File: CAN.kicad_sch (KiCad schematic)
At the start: 18 parts, among them J21 CAN_IN, J22 CAN_OUT, J26 CAN_TP, U17 ADM3055E, U18 CDSOT23-T24CAN

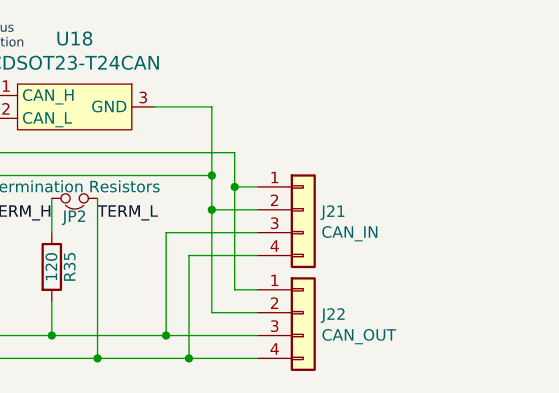
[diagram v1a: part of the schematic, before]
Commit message: Schematic notations for rework changes
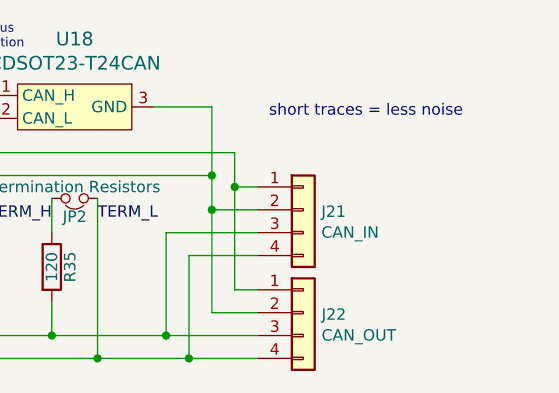
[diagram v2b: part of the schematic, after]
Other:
- note added: "short traces = less noise"

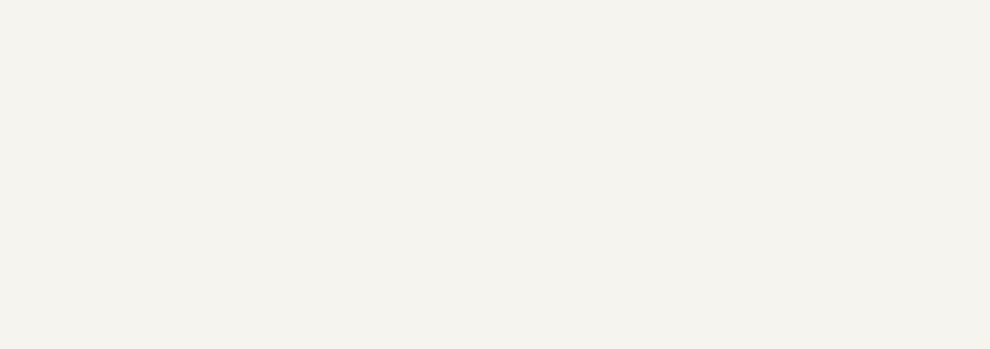
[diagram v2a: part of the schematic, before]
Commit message: Updated schematic in accordance to previous weeks annotated changes
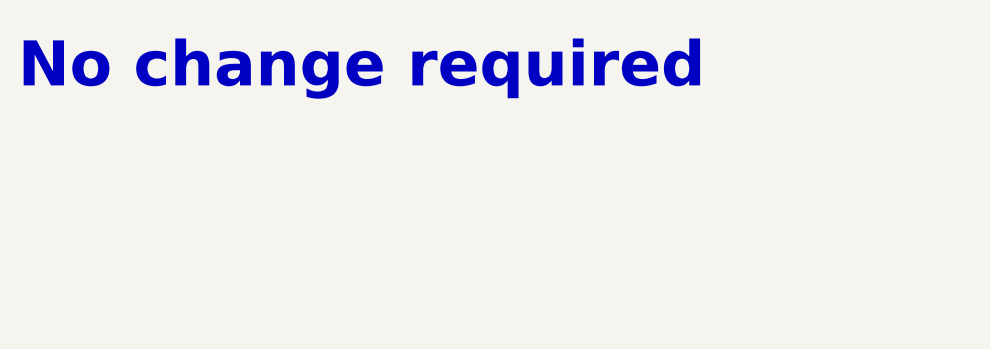
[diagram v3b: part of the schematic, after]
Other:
- note added: "No change required"
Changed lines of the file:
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@@
     (effects (font (size 1.016 1.016)) (justify left bottom))
+  )
+  (text "No change required\n" (at 15.24 21.59 0)
+    (effects (font (face "KiCad Font") (size 5 5) (thickness 1) bold (color 255 2 13 1)) (justify left bottom))
   )
   (label "TERM_L" (at 208.28 85.09 0) (fields_autoplaced)

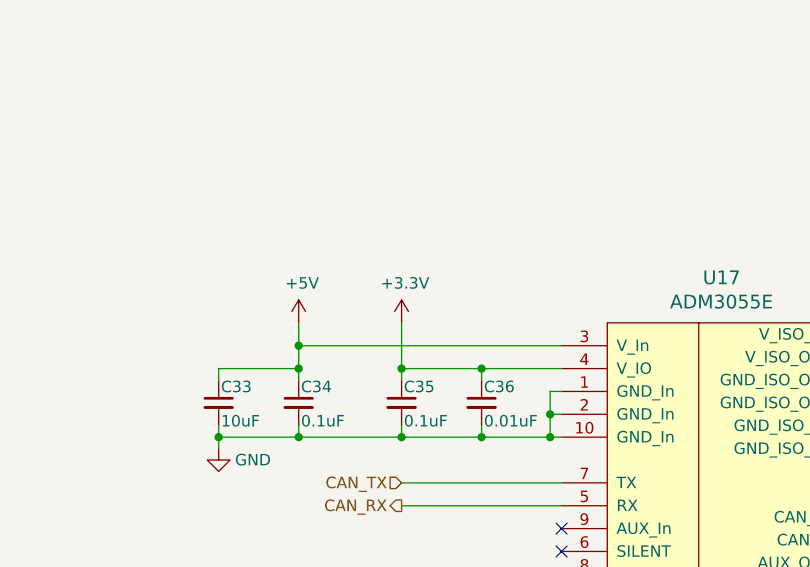
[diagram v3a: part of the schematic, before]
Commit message: Renamed Clk to PA5, removed CAN_TX/RX test points, deleted other .lck file and #auto_saved_files# (hopefully this does not break anything.
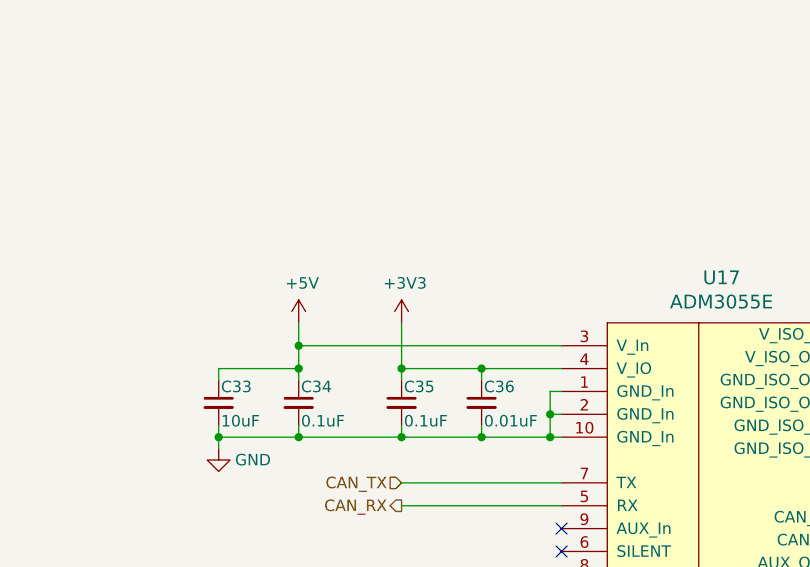
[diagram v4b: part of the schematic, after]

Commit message: Added/checked datasheet links/part numbers, deleted accel_pot2 and brake_pot2 hierarchical labels and changed corresponding pins (PC2, PC3) to GPIO on the now-2x5 extra GPIO connector.
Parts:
- C33, C38: Mouser Part Number 80-C0805C106K8RAUTO -> 963-TMK212BBJ106MGHT
- C34, C35, C39: Mouser Part Number 80-C0805C104K3R -> 80-C0805C104M5R
- C36, C40: Mouser Part Number 80-C0805X103K1R3316 -> C0805C103J5RACTU
- C37: Mouser Part Number 80-C0805C224J1RECTU -> 80-C0805C224J1RECTU
- R35: Mouser Part Number 71-CRCW080559R0FKEA -> CRCW0805120RFKEA
- U17: P/N (none) -> ADM3055E
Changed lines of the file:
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@@
 			)
 		)
-		(property "Datasheet" "~"
+		(property "Datasheet" "https://www.mouser.com/ProductDetail/71-CRCW0805120RFKEA"
 			(at 203.2 90.17 0)
 			(effects
@@
 			)
 		)
-		(property "Mouser Part Number" "71-CRCW080559R0FKEA"
+		(property "Mouser Part Number" "CRCW0805120RFKEA"
 			(at 203.2 90.17 0)
 			(effects
@@
 			)
 		)
-		(property "Datasheet" "~"
+		(property "Datasheet" "https://www.mouser.com/ProductDetail/TAIYO-YUDEN/TMK212BBJ106MGHT?qs=sGAEpiMZZMsh%252B1woXyUXj6Ion9DcW8uk%2FCsbgn7gICc%3D"
 			(at 54.61 85.09 0)
 			(effects
@@
 			)
 		)
-		(property "Mouser Part Number" "80-C0805C106K8RAUTO "
+		(property "Mouser Part Number" "963-TMK212BBJ106MGHT"
 			(at 54.61 85.09 0)
 			(effects
@@
 			)
 		)
-		(property "Datasheet" "~"
+		(property "Datasheet" "https://www.mouser.com/ProductDetail/KEMET/C0805C104M5RACTU?qs=VOOUd%252Bza08qHu13WgNByHQ%3D%3D"
 			(at 63.5 85.09 0)
 			(effects
@@
 			)
 		)
-		(property "Mouser Part Number" "80-C0805C104K3R "
+		(property "Mouser Part Number" "80-C0805C104M5R"
 			(at 63.5 85.09 0)
 			(effects
@@
 			)
 		)
-		(property "Datasheet" "~"
+		(property "Datasheet" "https://www.mouser.com/ProductDetail/KEMET/C0805C104M5RACTU?qs=VOOUd%252Bza08qHu13WgNByHQ%3D%3D"
 			(at 74.93 85.09 0)
 			(effects
@@
 			)
 		)
-		(property "Mouser Part Number" "80-C0805C104K3R "
+		(property "Mouser Part Number" "80-C0805C104M5R"
 			(at 74.93 85.09 0)
 			(effects
@@
 			)
 		)
-		(property "Datasheet" "~"
+		(property "Datasheet" "https://www.mouser.com/ProductDetail/KEMET/C0805C103J5RACTU?qs=Onq5MIl0ZjiJ615hCkQQ7A%3D%3D"
 			(at 83.82 85.09 0)
 			(effects
@@
 			)
 		)
-		(property "Mouser Part Number" "80-C0805X103K1R3316 "
+		(property "Mouser Part Number" "C0805C103J5RACTU"
 			(at 83.82 85.09 0)
 			(effects
@@
 			)
 		)
-		(property "Datasheet" "~"
+		(property "Datasheet" "https://www.mouser.com/ProductDetail/TAIYO-YUDEN/TMK212BBJ106MGHT?qs=sGAEpiMZZMsh%252B1woXyUXj6Ion9DcW8uk%2FCsbgn7gICc%3D"
 			(at 156.21 81.28 0)
 			(effects
@@
 			)
 		)
-		(property "Mouser Part Number" "80-C0805C106K8RAUTO "
+		(property "Mouser Part Number" "963-TMK212BBJ106MGHT"
 			(at 156.21 81.28 0)
 			(effects
@@
 			)
 		)
-		(property "Datasheet" "~"
+		(property "Datasheet" "https://www.mouser.com/ProductDetail/KEMET/C0805C224J1RECTU?qs=55YtniHzbhA8coEmCgZh4A%3D%3D&srsltid=AfmBOope8E98p1TAxytK4MEkGo55JjU107N1pzX-xa8_vzbWYaq6BWq_"
 			(at 146.05 81.28 0)
 			(effects
@@
 			)
 		)
-		(property "Mouser Part Number" "80-C0805C224J1RECTU "
+		(property "Mouser Part Number" "80-C0805C224J1RECTU"
 			(at 146.05 81.28 0)
 			(effects
@@
 			)
 		)
-		(property "Datasheet" ""
+		(property "Datasheet" "https://www.mouser.com/ProductDetail/TAIYO-YUDEN/BK2125LM182-T?qs=I6KAKw0tg2wTd%252Bj343lu1Q%3D%3D&srsltid=AfmBOorkhsm8Uk29brVkfBS5oJy8t8TPSw1gIhtEERu0OY8r33ydtYfJ"
 			(at 151.13 77.47 0)
 			(effects
@@
 			)
 		)
-		(property "Datasheet" ""
+		(property "Datasheet" "https://www.mouser.com/ProductDetail/TAIYO-YUDEN/BK2125LM182-T?qs=I6KAKw0tg2wTd%252Bj343lu1Q%3D%3D&srsltid=AfmBOorkhsm8Uk29brVkfBS5oJy8t8TPSw1gIhtEERu0OY8r33ydtYfJ"
 			(at 151.13 85.09 0)
 			(effects
@@
 			)
 		)
-		(property "Datasheet" "~"
+		(property "Datasheet" "https://www.mouser.com/ProductDetail/KEMET/C0805C104M5RACTU?qs=VOOUd%252Bza08qHu13WgNByHQ%3D%3D"
 			(at 166.37 81.28 0)
 			(effects
@@
 			)
 		)
-		(property "Mouser Part Number" "80-C0805C104K3R "
+		(property "Mouser Part Number" "80-C0805C104M5R"
 			(at 166.37 81.28 0)
 			(effects
@@
 			)
 		)
-		(property "Datasheet" "~"
+		(property "Datasheet" "https://www.mouser.com/ProductDetail/KEMET/C0805C103J5RACTU?qs=Onq5MIl0ZjiJ615hCkQQ7A%3D%3D"
 			(at 173.99 81.28 0)
 			(effects
@@
 			)
 		)
-		(property "Mouser Part Number" "80-C0805X103K1R3316 "
+		(property "Mouser Part Number" "C0805C103J5RACTU"
 			(at 173.99 81.28 0)
 			(effects
@@
 			)
 		)
-		(property "Datasheet" "~"
+		(property "Datasheet" "https://www.mouser.in/ProductDetail/Vishay-Dale/CRCW08050000Z0EAC?qs=E3Y5ESvWgWMnvHb9ZvShmA%3D%3D"
 			(at 140.97 105.41 0)
 			(effects
@@
 			(at 110.49 91.44 0)
 			(effects
+				(font
+					(size 1.27 1.27)
+				)
+				(hide yes)
+			)
+		)
+		(property "P/N" "ADM3055E"
+			(at 110.49 91.44 0)
+			(effects

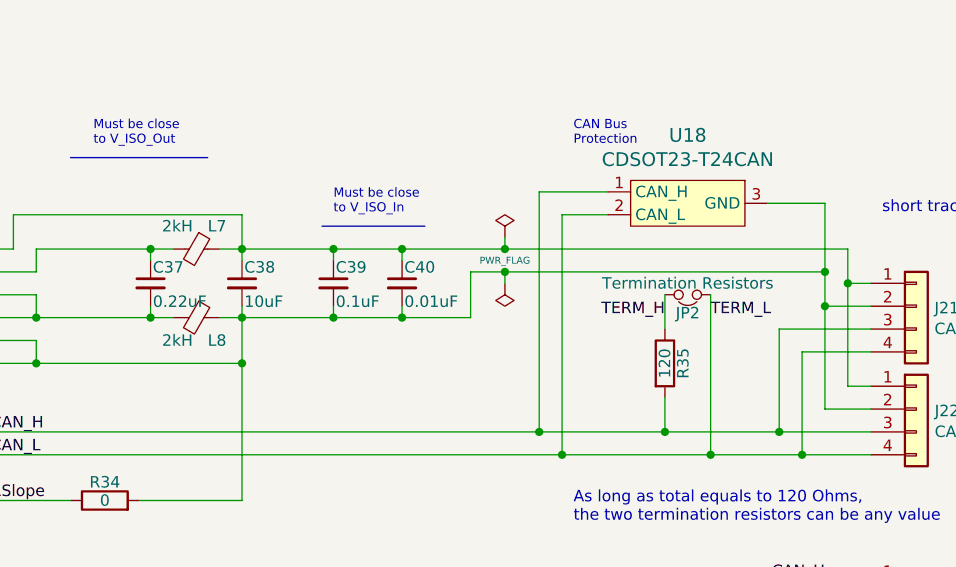
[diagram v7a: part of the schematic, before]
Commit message: Updated ferrite beads.
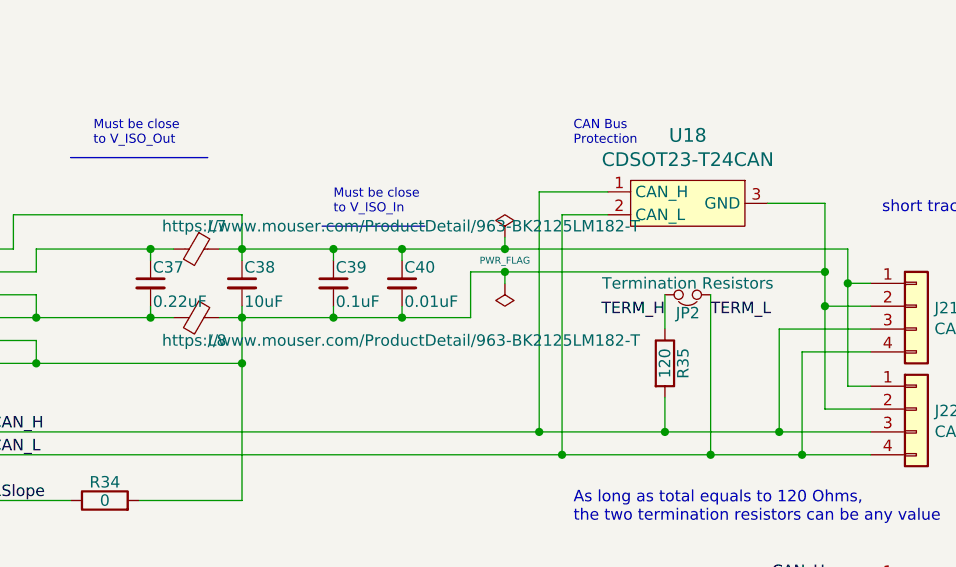
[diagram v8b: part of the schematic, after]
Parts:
- L7, L8: value 2kH -> https://www.mouser.com/ProductDetail/963-BK2125LM182-T; Mouser Part Number 963-BK2125LM182-T -> BKH1005LM182-T
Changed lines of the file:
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@@
 			)
 		)
-		(property "Value" "2kH"
+		(property "Value" "https://www.mouser.com/ProductDetail/963-BK2125LM182-T"
 			(at 147.32 74.93 90)
 			(effects
@@
 			)
 		)
-		(property "Mouser Part Number" "963-BK2125LM182-T "
+		(property "Mouser Part Number" "BKH1005LM182-T "
 			(at 151.13 77.47 0)
 			(effects
@@
 			)
 		)
-		(property "Value" "2kH"
+		(property "Value" "https://www.mouser.com/ProductDetail/963-BK2125LM182-T"
 			(at 147.32 87.63 90)
 			(effects
@@
 			)
 		)
-		(property "Mouser Part Number" "963-BK2125LM182-T "
+		(property "Mouser Part Number" "BKH1005LM182-T "
 			(at 151.13 85.09 0)
 			(effects
